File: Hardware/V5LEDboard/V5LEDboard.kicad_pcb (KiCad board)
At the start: 2 copper layers, 52.6 x 25.2 mm, 62 parts

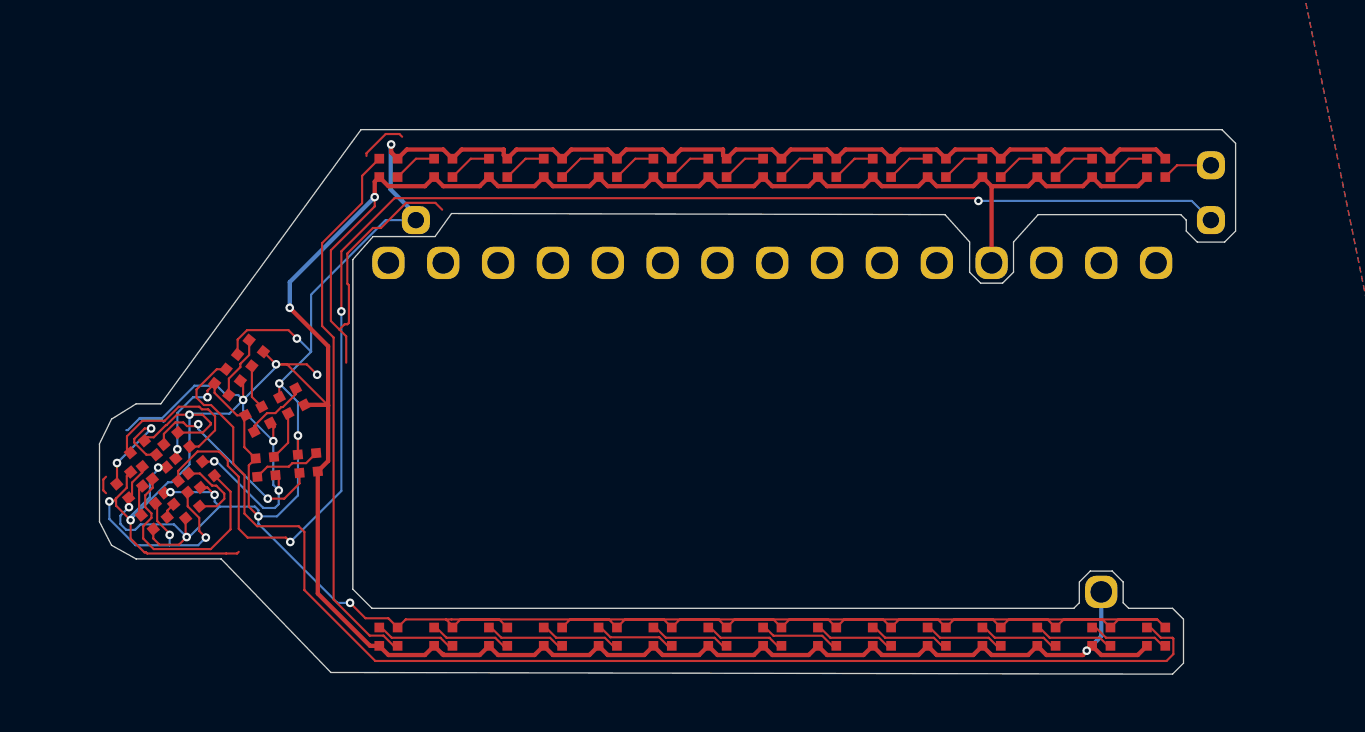
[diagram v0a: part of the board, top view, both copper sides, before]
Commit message: Now with RP2350B!
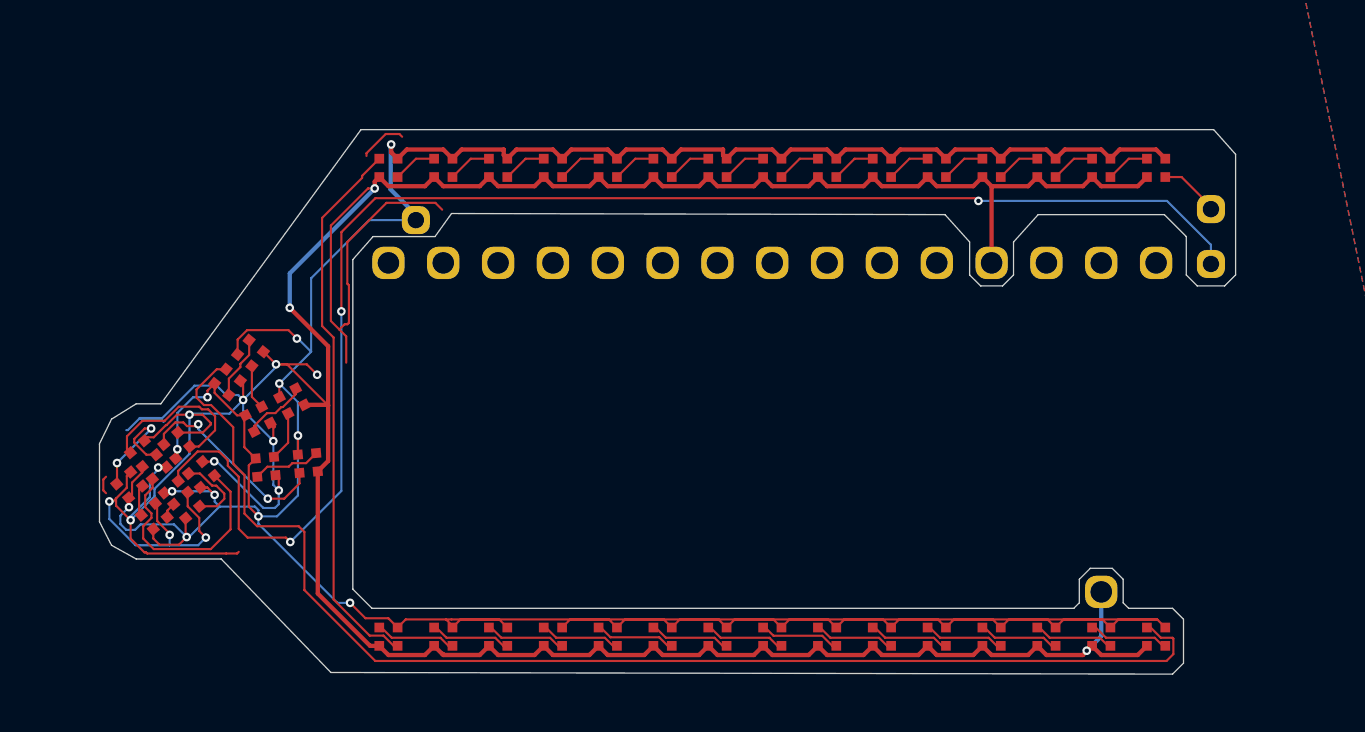
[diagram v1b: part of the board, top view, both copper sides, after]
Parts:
- moved TP1 2.03 mm to (161.3, 86.4)
- moved TP5 2.03 mm to (161.3, 89.0)
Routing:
- net Net-(D43-DOUT): track 65.5 -> 67.4 mm
- net GND: track 205.9 -> 206.7 mm
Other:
- outline, holes or cut-outs redrawn

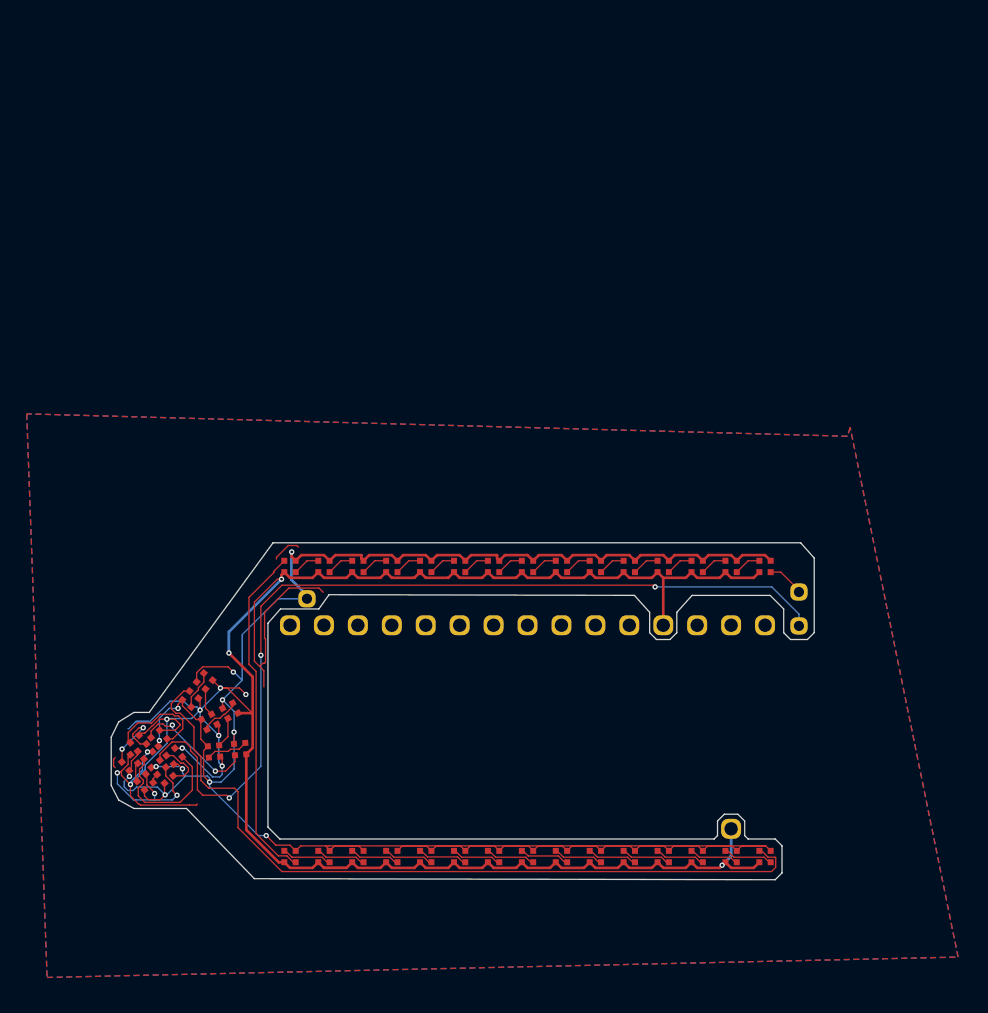
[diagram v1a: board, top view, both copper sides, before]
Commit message: Fixed lockups - added Apps to Menu - routed 23V50
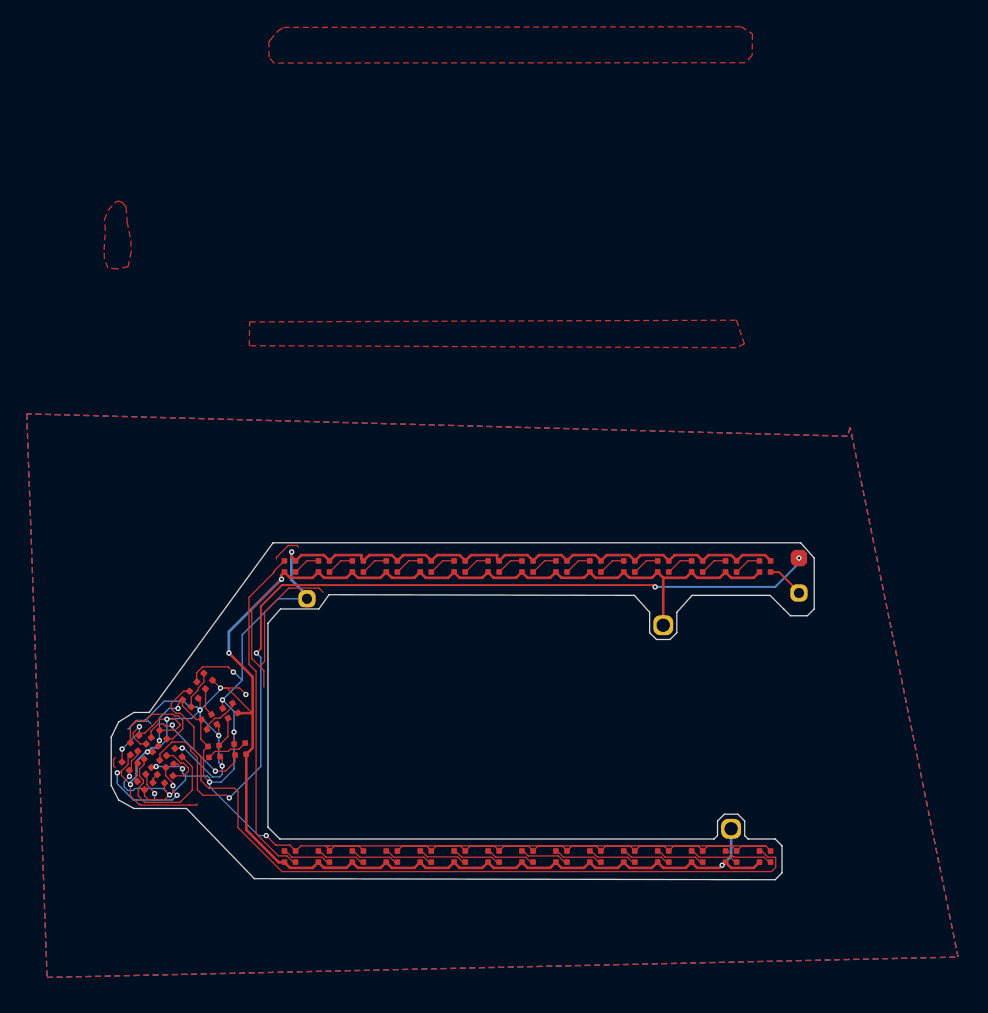
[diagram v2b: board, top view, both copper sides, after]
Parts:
- removed the TP3 at (143.5, 88.9)
- removed the TP3 at (158.8, 88.9)
- removed the TP3 at (130.8, 88.9)
- removed the TP3 at (125.7, 88.9)
- removed the TP3 at (148.6, 88.9)
- removed the TP3 at (156.2, 88.9)
- removed the TP3 at (135.9, 88.9)
- removed the TP3 at (146.1, 88.9)
- removed the TP3 at (133.3, 88.9)
- removed the TP3 at (138.4, 88.9)
- removed the TP3 at (123.2, 88.9)
- removed the TP3 at (128.3, 88.9)
- removed the TP3 at (153.7, 88.9)
- removed the TP3 at (141.0, 88.9)
- added REF**: Minimum_CE_Mark, JumperlessFootprints:Minimum_CE_Mark, B.Cu at (118.1, 93.7)
- TP5: footprint JumperlessFootprints:PINHEADER-1x1_vertical -> JumperlessFootprints:TestPoint_D0.75mm
- moved TP5 5.08 mm to (161.3, 83.9)
- moved TP1 0.08 mm to (161.3, 86.5)
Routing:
- net GND: track 206.7 -> 205.9 mm, vias 15 -> 16
- net +5V: track 180.1 -> 180.6 mm
- net Net-(D43-DOUT): track 67.4 -> 67.0 mm, vias 3 -> 4
- added copper zone on F.Cu, net (none)
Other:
- outline, holes or cut-outs redrawn

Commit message: pulled out dome debug prints, fixed fab complaints
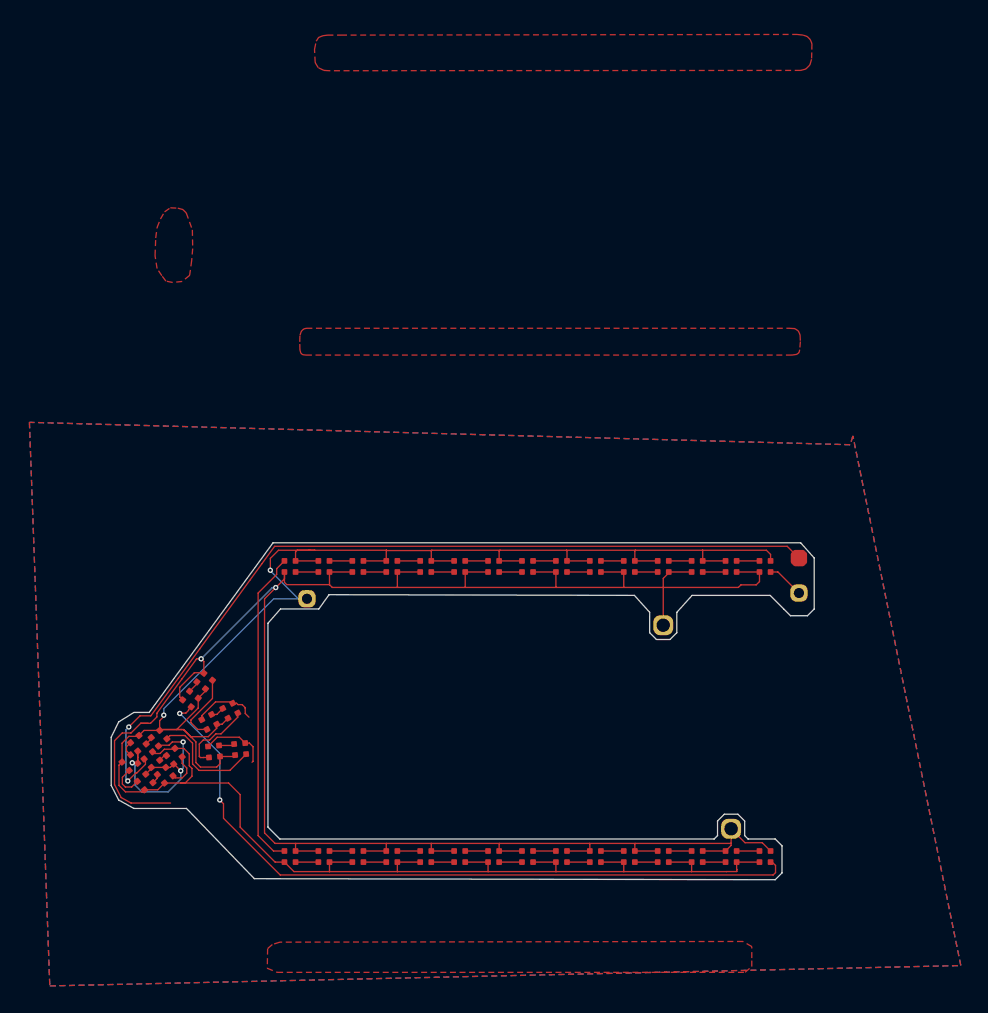
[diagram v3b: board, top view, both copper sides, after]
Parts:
- turned D10 to 90 degrees
- turned D12 to 90 degrees
- turned D14 to 90 degrees
- turned D16 to 180 degrees
- turned D17 to -90 degrees
- turned D18 to 180 degrees
- turned D19 to -90 degrees
- turned D2 to 90 degrees
- turned D20 to 180 degrees
- turned D21 to -90 degrees
- turned D22 to 180 degrees
- turned D23 to -90 degrees
- turned D24 to 180 degrees
- turned D25 to -90 degrees
- turned D26 to 180 degrees
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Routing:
- net GND: track 205.9 -> 192.1 mm, vias 16 -> 5
- net Net-(D42-DOUT): track 10.6 -> 0.65 mm
- net Net-(D37-DOUT): track 7.85 -> 0.63 mm
- net +5V: track 180.6 -> 176.4 mm, vias 12 -> 2
- net Net-(D38-DOUT): track 5.35 -> 1.32 mm, vias 2 -> 0
- net Net-(D30-DOUT): track 58.3 -> 54.5 mm, vias 0 -> 2
- net Net-(D34-DOUT): track 2.28 -> 5.72 mm
- net Net-(D43-DOUT): track 67.0 -> 63.8 mm, vias 4 -> 2
- net Net-(D32-DOUT): track 2.08 -> 5.25 mm
- net Net-(D28-DOUT): track 3.74 -> 1.71 mm
- net Net-(D24-DOUT): track 3.74 -> 1.71 mm
- net Net-(D21-DOUT): track 3.74 -> 1.71 mm
- net Net-(D19-DOUT): track 3.74 -> 1.71 mm
- net Net-(D18-DOUT): track 3.74 -> 1.71 mm
- net Net-(D16-DOUT): track 3.74 -> 1.71 mm
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
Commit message: Rev 4 hardware
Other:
- board size 52.6 x 25.2 mm -> 57.1 x 26.1 mm
